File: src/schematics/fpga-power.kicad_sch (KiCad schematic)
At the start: 25 parts

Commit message: Updates the root page
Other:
- removed sheet FPGA Bank 0
- removed sheet FPGA Bank 1
- removed sheet FPGA Bank 2
- removed sheet FPGA Bank 3
- removed sheet FPGA Bank 4
- removed sheet FPGA Bank 6
- removed sheet FPGA Bank 7
- removed sheet FPGA Bank 8
- note removed: "JTAG"
- moved on the sheet: C24, C25, C26, C27, C28, C29, C30, C31, C32, C33, C34, C35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

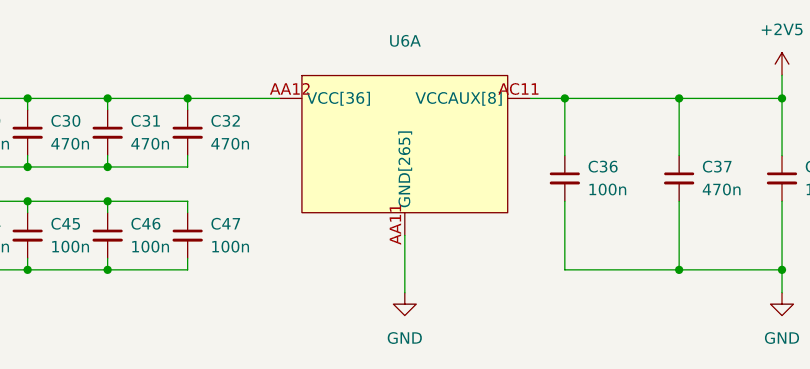
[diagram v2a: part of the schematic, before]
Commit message: ✅ Validate the schematic symbols (#33)
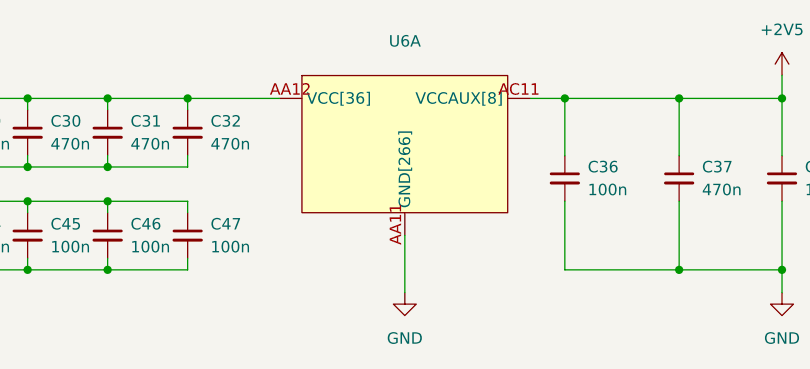
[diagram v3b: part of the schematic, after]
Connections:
- net GND: now also U6.P20 (GND), U6.R11 (GND)
- new net: U6.AC29 (NC), U6.AC4 (NC), U6.AE26 (NC), U6.AE7 (NC), U6.AG2 (NC), U6.AG24 (NC), U6.AG31 (NC), U6.E26 (NC), U6.E7 (NC), U6.G10 (NC), U6.G11 (NC), U6.G14 (NC), U6.G15 (NC), U6.G16 (NC), U6.G17 (NC), U6.G18 (NC), U6.G19 (NC), U6.G22 (NC), U6.G23 (NC), U6.G24 (NC), U6.G9 (NC), U6.H29 (NC), U6.H4 (NC), U6.L28 (NC), U6.L5 (NC), U6.V3 (NC), U6.V30 (NC), U6.W27 (NC), U6.W6 (NC)
- new net: U6.AK10 (RESERVED), U6.AK12 (RESERVED), U6.AK13 (RESERVED), U6.AK15 (RESERVED), U6.AK16 (RESERVED), U6.AK18 (RESERVED), U6.AK19 (RESERVED), U6.AK21 (RESERVED), U6.AK22 (RESERVED), U6.AK24 (RESERVED), U6.AK25 (RESERVED), U6.AK9 (RESERVED)
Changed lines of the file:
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@@
 		(pin "AM4"
+		)
+		(pin "AG24"
+		)
+		(pin "AC29"
+		)
+		(pin "AC4"
+		)
+		(pin "AE26"
+		)
+		(pin "AE7"
+		)
+		(pin "AG2"
+		)
+		(pin "AG31"
+		)
+		(pin "AK10"
+		)
+		(pin "AK12"
+		)
+		(pin "AK13"
+		)
+		(pin "AK15"
+		)
+		(pin "AK16"
+		)
+		(pin "AK18"
+		)
+		(pin "AK19"
+		)
+		(pin "AK21"
+		)
+		(pin "AK22"
+		)
+		(pin "AK24"
+		)
+		(pin "AK25"
+		)
+		(pin "AK9"
+		)
+		(pin "E26"
+		)
+		(pin "E7"
+		)
+		(pin "G10"
+		)
+		(pin "G11"
+		)
+		(pin "G14"
+		)
+		(pin "G15"
+		)
+		(pin "G16"
+		)
+		(pin "G17"
+		)
+		(pin "G18"
+		)
+		(pin "G19"
+		)
+		(pin "G22"
+		)
+		(pin "G23"
+		)
+		(pin "G24"
+		)
+		(pin "G9"
+		)
+		(pin "H29"
+		)
+		(pin "H4"
+		)
+		(pin "L28"
+		)
+		(pin "L5"
+		)
+		(pin "P20"
+		)
+		(pin "R11"
+		)
+		(pin "V3"
+		)
+		(pin "V30"
+		)
+		(pin "W27"
+		)
+		(pin "W6"
+		)
+		(pin "AG5"
+		)
+		(pin "AJ5"
+		)
+		(pin "AK5"
+		)
+		(pin "AM5"
 		)
 		(instances

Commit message: Add footprint for ecp5 (#75)
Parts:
- U6: footprint (none) -> ECAP5-DPROC:LFE5U-85F-_BG756C
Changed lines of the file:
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@@
 			)
 		)
-		(property "Footprint" ""
+		(property "Footprint" "ECAP5-DPROC:LFE5U-85F-_BG756C"
 			(at 189.23 81.28 0)
 			(effects

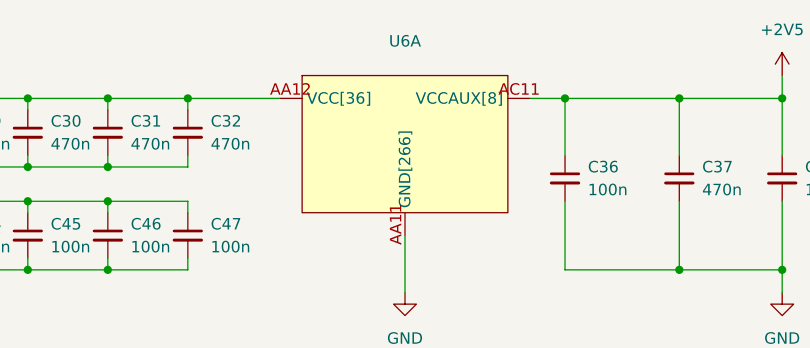
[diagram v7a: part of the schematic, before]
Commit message: Add footprint for the io connector
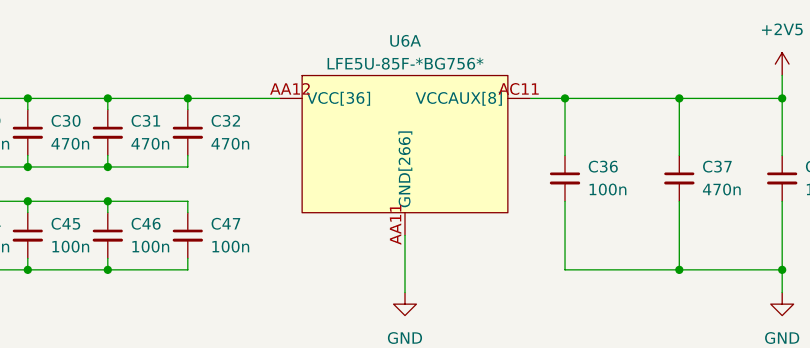
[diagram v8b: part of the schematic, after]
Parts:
- U6: value ~ -> LFE5U-85F-*BG756*
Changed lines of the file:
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@@
 			)
 		)
-		(property "Value" "~"
+		(property "Value" "LFE5U-85F-*BG756*"
 			(at 196.85 77.47 0)
 			(effects
